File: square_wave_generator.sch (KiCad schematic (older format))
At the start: 8 parts, among them U1 NE555, U2 IXDF604SIA

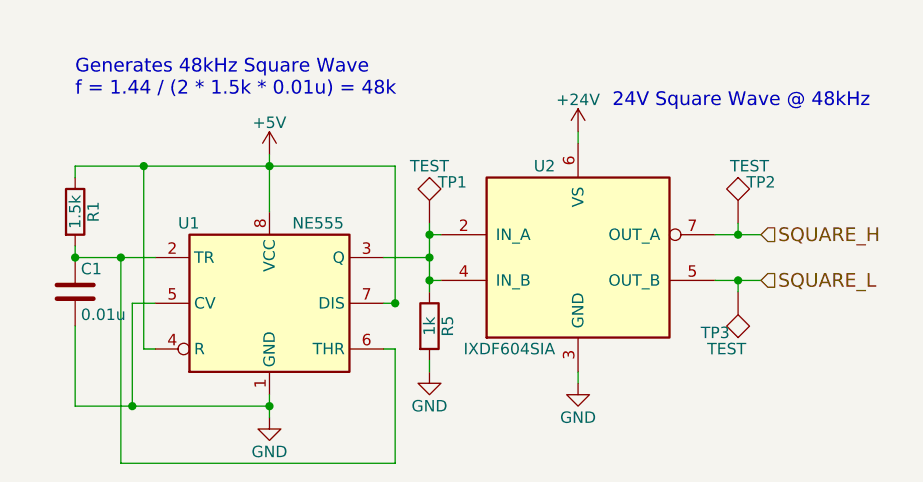
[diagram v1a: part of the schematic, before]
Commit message: Changed 555 timer configuration.
555 timer was not behaving correctly. Added resistor to out for timing and increased resistor to 5V to mostly open circuit (in steady state).

Added extra coupling capacitor for control voltage.
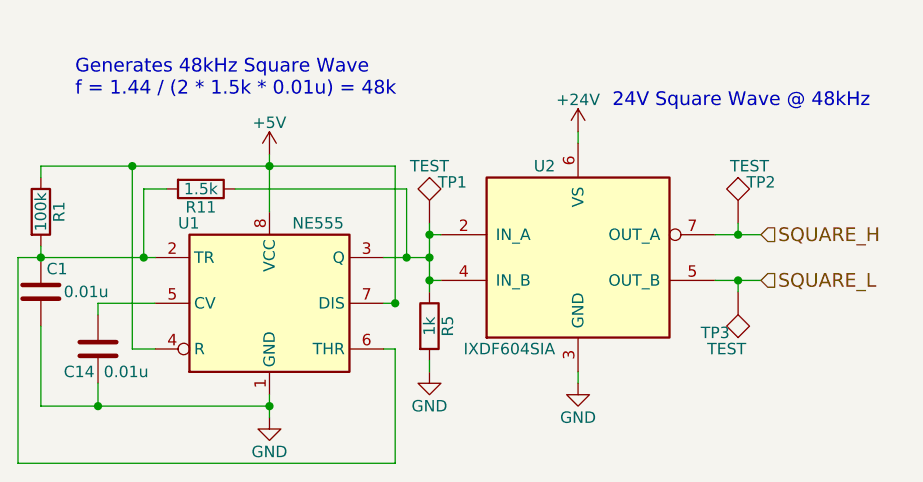
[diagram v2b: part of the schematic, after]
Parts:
- added C14: 0.01u, Capacitors_SMD:C_0603_HandSoldering, symbol C
- added R11: 1.5k, symbol R
- R1: value 1.5k -> 100k
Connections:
- net GND: now also C14.2; no longer U1.5 (CV)
- net at R5.1, TP1.1, U1.3 (Q)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: now also R11.1
- net at C1.1, R1.2, U1.2 (TR)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: now also R11.2
- new net: C14.1, U1.5 (CV)
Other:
- moved on the sheet: C1, R1
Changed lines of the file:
@@
 L R R1
 U 1 1 5ADB7815
-P 1850 2250
-F 0 "R1" V 1930 2250 50  0000 C CNN
-F 1 "1.5k" V 1850 2250 50  0000 C CNN
-F 2 "Resistors_SMD:R_0603_HandSoldering" V 1780 2250 50  0001 C CNN
-F 3 "" H 1850 2250 50  0001 C CNN
-	1    1850 2250
+P 1700 2250
+F 0 "R1" V 1780 2250 50  0000 C CNN
+F 1 "100k" V 1700 2250 50  0000 C CNN
+F 2 "Resistors_SMD:R_0603_HandSoldering" V 1630 2250 50  0001 C CNN
+F 3 "" H 1700 2250 50  0001 C CNN
+	1    1700 2250
 	1    0    0    -1
 $EndComp
@@
 L C C1
 U 1 1 5ADB781C
-P 1850 2600
-F 0 "C1" H 1875 2700 50  0000 L CNN
-F 1 "0.01u" H 1875 2500 50  0000 L CNN
-F 2 "Capacitors_SMD:C_0603_HandSoldering" H 1888 2450 50  0001 C CNN
-F 3 "" H 1850 2600 50  0001 C CNN
-	1    1850 2600
+P 1700 2600
+F 0 "C1" H 1725 2700 50  0000 L CNN
+F 1 "0.01u" H 1800 2600 50  0000 L CNN
+F 2 "Capacitors_SMD:C_0603_HandSoldering" H 1738 2450 50  0001 C CNN
+F 3 "" H 1700 2600 50  0001 C CNN
+	1    1700 2600
 	1    0    0    -1
 $EndComp
@@
 	4650 2350 4850 2350
 Wire Wire Line
-	4850 2550 4650 2550
+	4650 2550 4850 2550
 Wire Wire Line
 	4050 2950 4050 3000
@@
 	2700 3050 2700 3150
 Wire Wire Line
-	2150 2850 2200 2850
+	2100 2850 2200 2850
 Wire Wire Line
-	1850 2050 3250 2050
+	1700 2050 3250 2050
 Wire Wire Line
-	2150 2050 2150 2850
+	2100 2050 2100 2850
 Connection ~ 3400 2450
 Wire Wire Line
-	2200 2650 2100 2650
-Wire Wire Line
-	2100 2650 2100 3100
+	2200 2650 1950 2650
 Connection ~ 2700 2050
 Wire Wire Line
-	1850 3100 2700 3100
+	1700 3100 2700 3100
 Connection ~ 2700 3100
 Wire Wire Line
@@
 	3250 2850 3250 3350
 Wire Wire Line
-	3250 3350 2050 3350
+	3250 3350 1600 3350
 Wire Wire Line
-	2050 3350 2050 2450
+	2150 2450 2150 2150
 Wire Wire Line
-	1850 2450 2200 2450
+	1600 2450 2200 2450
 Wire Wire Line
 	3200 2650 3250 2650
 Wire Wire Line
 	3250 2650 3250 2050
-Connection ~ 2050 2450
+Connection ~ 2150 2450
 Wire Wire Line
-	1850 2400 1850 2450
-Connection ~ 1850 2450
+	1700 2400 1700 2450
+Connection ~ 1700 2450
 Connection ~ 3250 2650
 Wire Wire Line
-	1850 2750 1850 3100
-Connection ~ 2100 3100
+	1700 2750 1700 3100
 Wire Wire Line
-	1850 2100 1850 2050
-Connection ~ 2150 2050
+	1700 2100 1700 2050
+Connection ~ 2100 2050
 Wire Wire Line
 	3200 2450 3400 2450
@@
 	4750 2550 4750 2600
 Connection ~ 4750 2550
+$Comp
+L R R11
+U 1 1 5AF44B07
+P 2400 2150
+F 0 "R11" V 2480 2150 50  0000 C CNN
+F 1 "1.5k" V 2400 2150 50  0000 C CNN
+F 2 "" V 2330 2150 50  0001 C CNN
+F 3 "" H 2400 2150 50  0001 C CNN
+	1    2400 2150
+	0    1    1    0
+$EndComp
+Wire Wire Line
+	2150 2150 2250 2150
+Wire Wire Line
+	2550 2150 3300 2150
+Wire Wire Line
+	3300 2150 3300 2450
+Connection ~ 3300 2450
+$Comp
+L C C14
+U 1 1 5AF45E29
+P 1950 2850
+F 0 "C14" H 1800 2750 50  0000 L CNN
+F 1 "0.01u" H 1975 2750 50  0000 L CNN
+F 2 "Capacitors_SMD:C_0603_HandSoldering" H 1988 2700 50  0001 C CNN
+F 3 "" H 1950 2850 50  0001 C CNN
+	1    1950 2850
+	1    0    0    -1
+$EndComp
+Wire Wire Line
+	1950 2650 1950 2700
+Wire Wire Line
+	1950 3000 1950 3100
+Connection ~ 1950 3100
+Wire Wire Line
+	1600 3350 1600 2450
 $EndSCHEMATC

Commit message: Adds NTC to connector.
Completes 555 rewire.

Rewires IGBT signals to layout more simply.
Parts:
- R11: footprint (none) -> Resistors_SMD:R_0603_HandSoldering
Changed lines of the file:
@@
 F 0 "R11" V 2480 2150 50  0000 C CNN
 F 1 "1.5k" V 2400 2150 50  0000 C CNN
-F 2 "" V 2330 2150 50  0001 C CNN
+F 2 "Resistors_SMD:R_0603_HandSoldering" V 2330 2150 50  0001 C CNN
 F 3 "" H 2400 2150 50  0001 C CNN
 	1    2400 2150

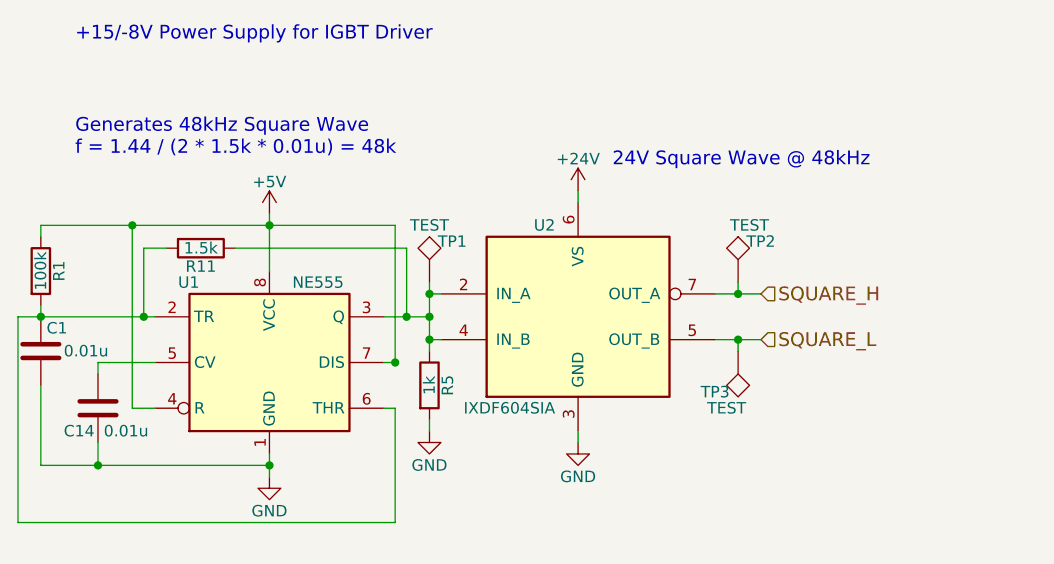
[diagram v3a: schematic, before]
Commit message: Changing 555 timer again to remove pullup resistor and discharge.
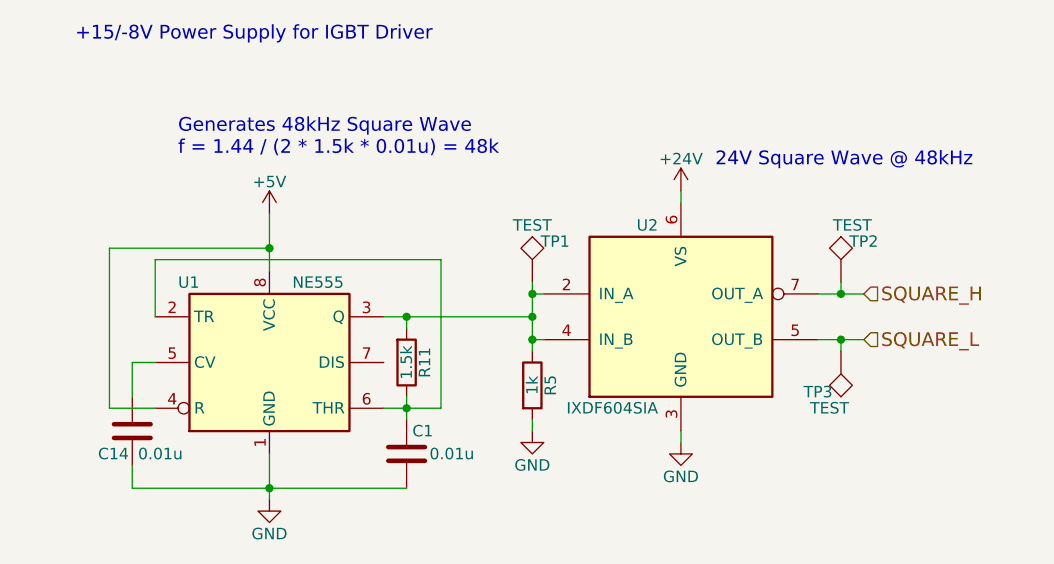
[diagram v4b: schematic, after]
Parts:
- removed R1: 100k, Resistors_SMD:R_0603_HandSoldering, symbol R
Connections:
- net +5V: no longer U1.7 (DIS)
- net at R5.1, TP1.1, U1.3 (Q)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: now also R11.2; no longer R11.1
- net at C1.1, U1.2 (TR), U1.6 (THR): now also R11.1; no longer R11.2
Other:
- moved on the sheet: C1, C14, R11, R5, TP1, TP2, TP3, U2

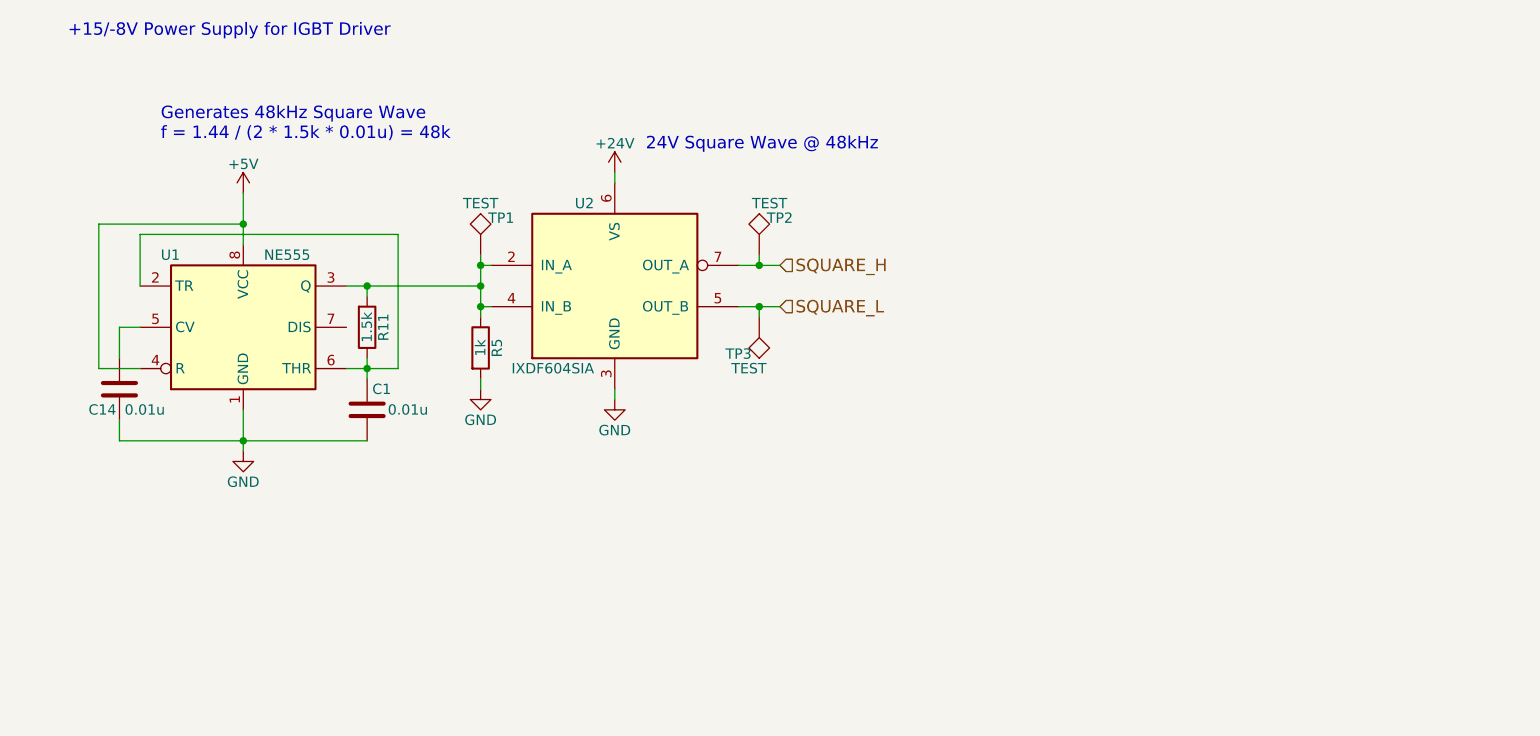
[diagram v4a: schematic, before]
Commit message: Adding d-flop to achieve 50% duty cycle
555 timer config cannot guarantee 50% duty cycle, but a frequency divider can.
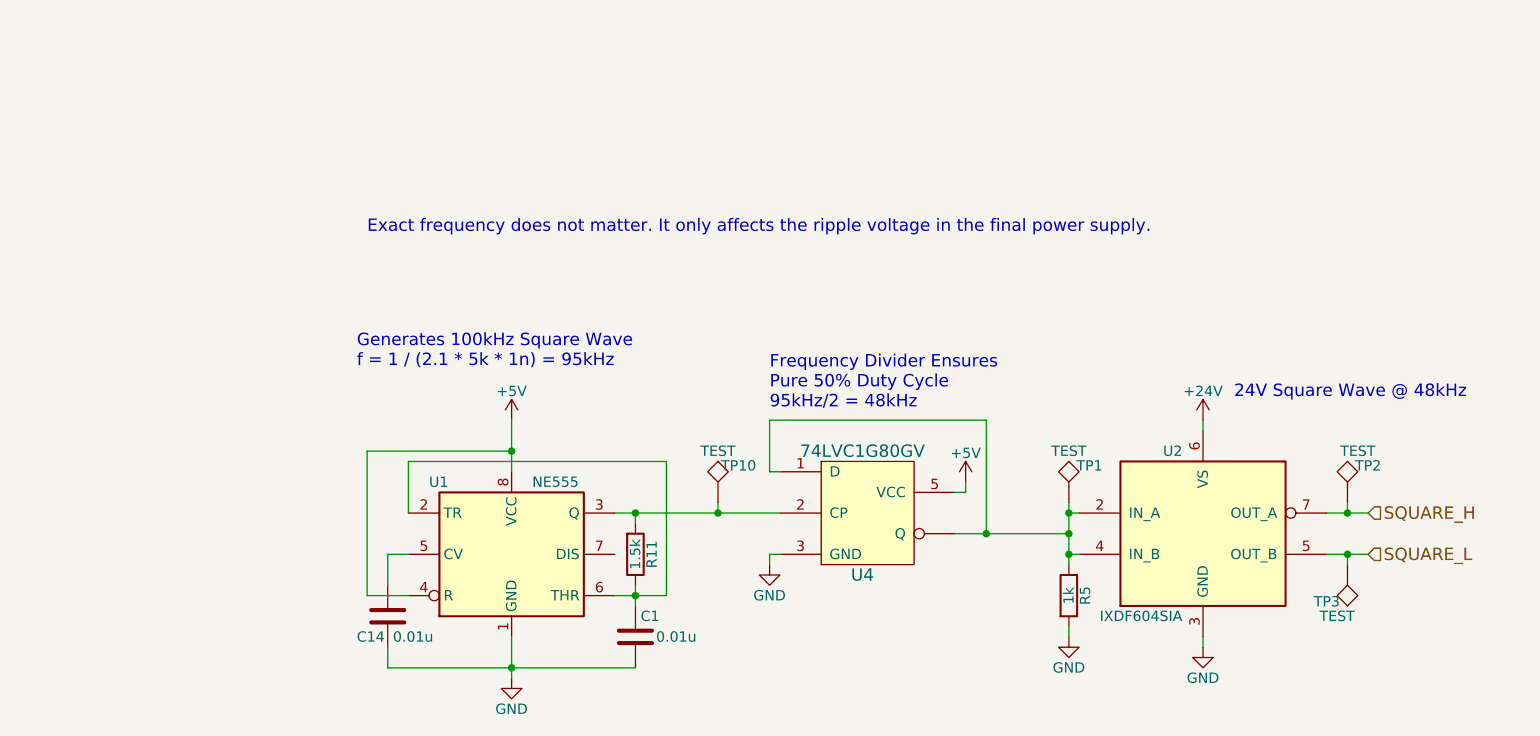
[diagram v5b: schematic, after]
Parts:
- added TP10: TEST, inverter-igbt-driver:TP RCT (0805), symbol TEST
- added U4: 74LVC1G80GV, TO_SOT_Packages_SMD:SOT-353_SC-70-5_Handsoldering, symbol 74LVC1G80GV
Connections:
- net +5V: now also U4.5 (VCC)
- net GND: now also U4.3 (GND)
- net at R5.1, TP1.1, U2.2 (IN_A)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: now also U4.1 (D), U4.~ (Q); no longer R11.2, U1.3 (Q)
- new net: R11.2, TP10.1, U1.3 (Q), U4.2 (CP)
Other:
- note added: "Exact frequency does not matter. It only affects the ripple voltage in the final power supply."
- note added: "Frequency Divider Ensures\nPure 50% Duty Cycle\n95kHz/2 = 48kHz"
- note added: "Generates 100kHz Square Wave\nf = 1 / (2.1 * 5k * 1n) = 95kHz"
- note removed: "+15/-8V Power Supply for IGBT Driver\n"
- note removed: "Generates 48kHz Square Wave\nf = 1.44 / (2 * 1.5k * 0.01u) = 48k"
- moved on the sheet: C1, C14, R11, R5, TP1, TP2, TP3, U1, U2

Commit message: Adjust resistor value and cap values for pulse generator
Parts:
- C1: value 0.01u -> 0.001n
- R11: value 1.5k -> 5.6k
- U4: symbol 74LVC1G80GV -> 74LVC1G80GV-RESCUE-inverter-igbt-driver
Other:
- note added: "Frequency Divider Ensures\nPure 50% Duty Cycle\n85kHz/2 = 43kHz"
- note added: "Generates 100kHz Square Wave\nf = 1 / (2.1 * 5.6k * 1n) = 85kHz"
- note removed: "Frequency Divider Ensures\nPure 50% Duty Cycle\n95kHz/2 = 48kHz"
- note removed: "Generates 100kHz Square Wave\nf = 1 / (2.1 * 5k * 1n) = 95kHz"
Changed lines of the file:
@@
 EESchema Schematic File Version 2
+LIBS:inverter-igbt-driver-rescue
 LIBS:power
 LIBS:device
@@
 P 4600 4150
 F 0 "C1" H 4625 4250 50  0000 L CNN
-F 1 "0.01u" H 4700 4150 50  0000 L CNN
+F 1 "0.001n" H 4700 4150 50  0000 L CNN
 F 2 "Capacitors_SMD:C_0603_HandSoldering" H 4638 4000 50  0001 C CNN
 F 3 "" H 4600 4150 50  0001 C CNN
@@
 $EndComp
 Text Notes 3250 2850 0    60   ~ 0
-Generates 100kHz Square Wave\nf = 1 / (2.1 * 5k * 1n) = 95kHz
+Generates 100kHz Square Wave\nf = 1 / (2.1 * 5.6k * 1n) = 85kHz
 Text Notes 7500 3000 0    60   ~ 0
 24V Square Wave @ 48kHz
@@
 P 4600 3750
 F 0 "R11" V 4680 3750 50  0000 C CNN
-F 1 "1.5k" V 4600 3750 50  0000 C CNN
+F 1 "5.6k" V 4600 3750 50  0000 C CNN
 F 2 "Resistors_SMD:R_0603_HandSoldering" V 4530 3750 50  0001 C CNN
 F 3 "" H 4600 3750 50  0001 C CNN
@@
 	4750 3300 4750 3950
 $Comp
-L 74LVC1G80GV U4
+L 74LVC1G80GV-RESCUE-inverter-igbt-driver U4
 U 1 1 5AF20A3C
 P 5700 3550
+AR Path="/5AF20A3C" Ref="U4"  Part="1"
+AR Path="/5ADB7652/5AF20A3C" Ref="U4"  Part="1"
 F 0 "U4" H 5700 3250 60  0000 C CNN
 F 1 "74LVC1G80GV" H 5700 3850 60  0000 C CNN
@@
 	5250 3350 5300 3350
 Text Notes 5250 3050 0    60   ~ 0
-Frequency Divider Ensures\nPure 50% Duty Cycle\n95kHz/2 = 48kHz
+Frequency Divider Ensures\nPure 50% Duty Cycle\n85kHz/2 = 43kHz
 $Comp
 L +5V #PWR012
